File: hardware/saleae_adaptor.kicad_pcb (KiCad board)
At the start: 2 copper layers, 50.8 x 31.8 mm, 18 parts, among them J1 Conn_01x12, J2 Conn_02x05_Odd_Even

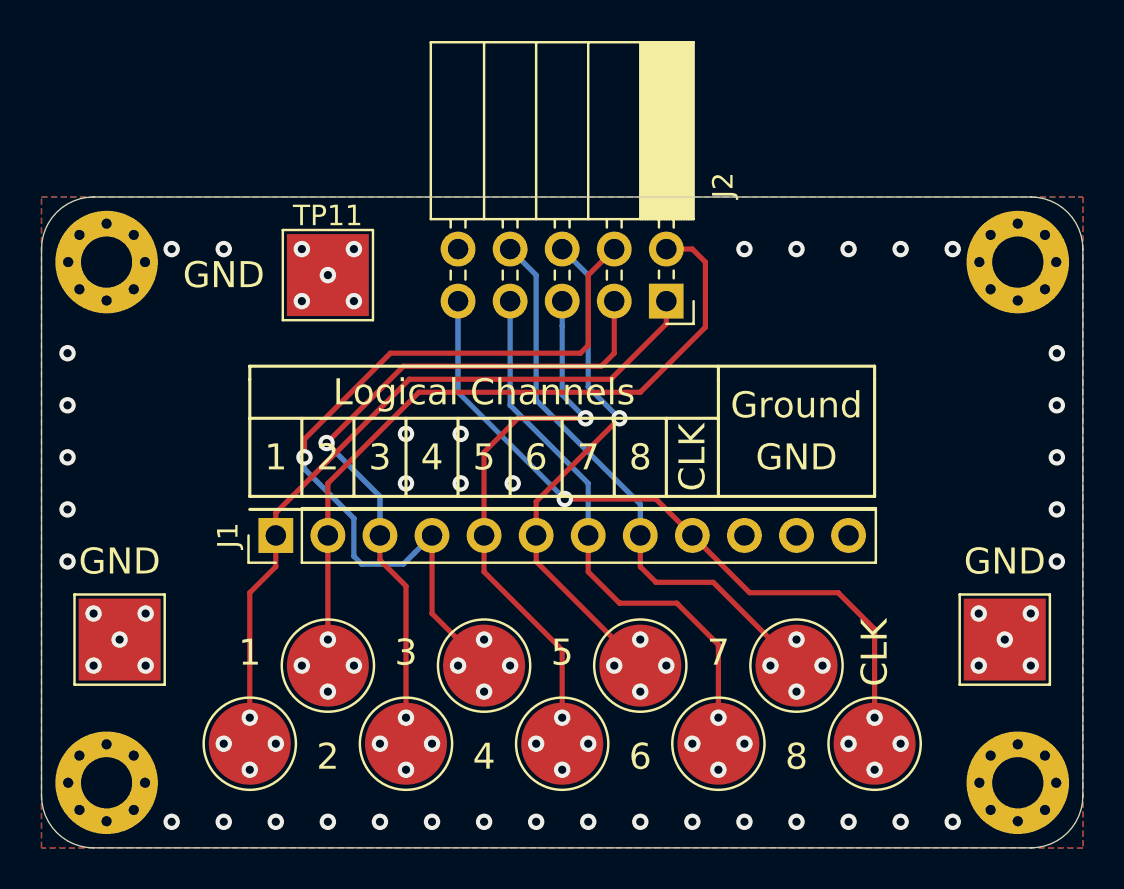
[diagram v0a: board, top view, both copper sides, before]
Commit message: Added new GND pad
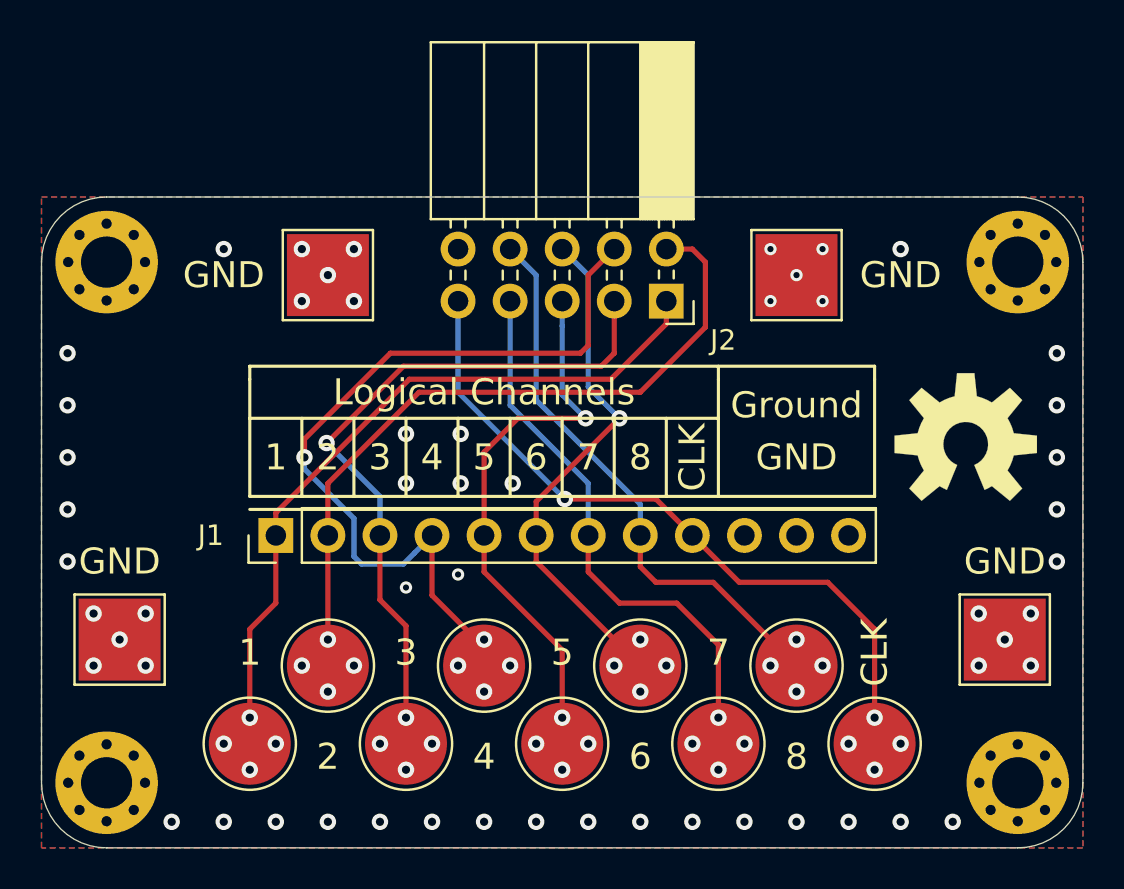
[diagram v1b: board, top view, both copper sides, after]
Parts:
- added ?: , Aesthetics:OSHW-LOGO-L, F.Cu at (160.7, 42.5)
- added TP13: GND, TestPoint:TestPoint_Pad_4.0x4.0mm, F.Cu at (152.4, 34.3)
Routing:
- net GND: vias 53 -> 55
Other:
- outline, holes or cut-outs redrawn
